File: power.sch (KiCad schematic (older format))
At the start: 51 parts, among them J301 BAT, J302 BAT, J304 SYS, U301 TPS560430X3F, U302 BQ25792

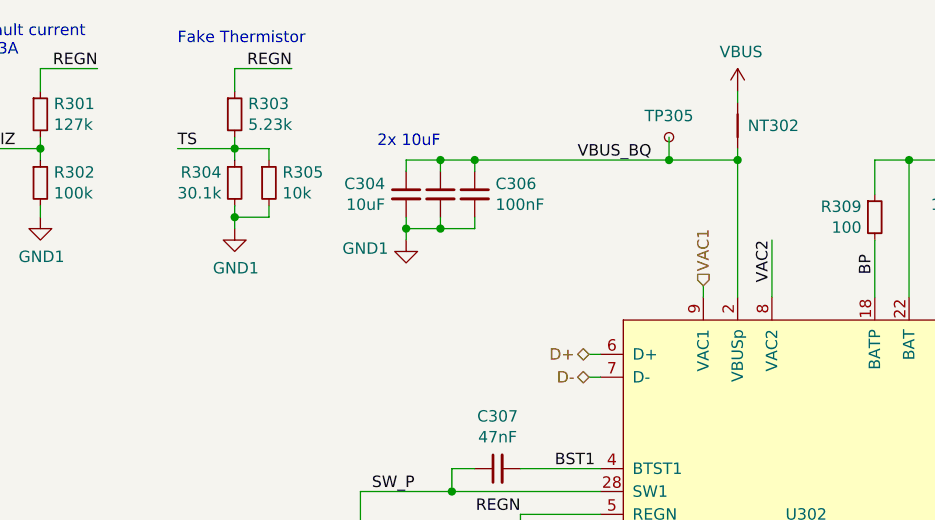
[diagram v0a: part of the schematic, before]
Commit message: added missing JLC/LCSC parts
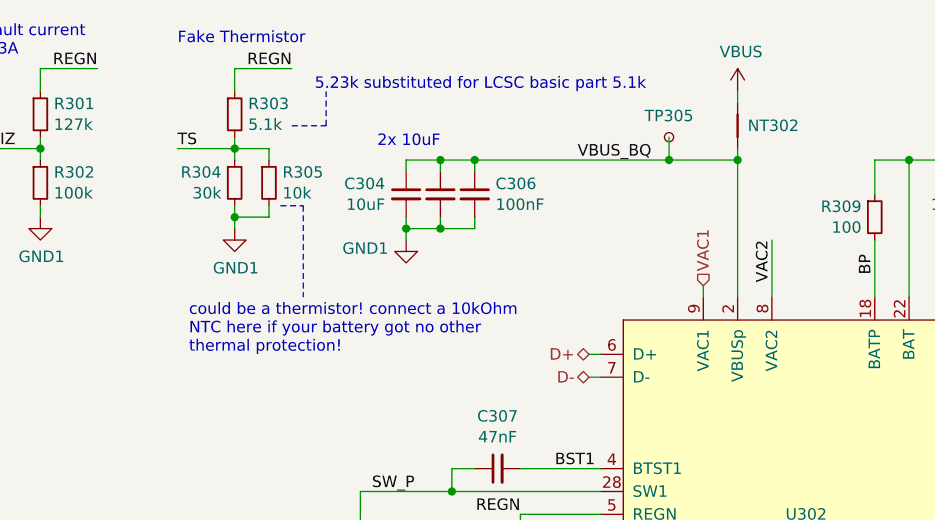
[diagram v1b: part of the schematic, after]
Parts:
- R303: value 5.23k -> 5.1k; JLC (none) -> 0603; LCSC (none) -> C23186
- R304: value 30.1k -> 30k; JLC (none) -> 0603; LCSC (none) -> C22984
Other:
- note added: "5.23k substituted for LCSC basic part 5.1k"
- note added: "could be a thermistor! connect a 10kOhm\nNTC here if your battery got no other\nthermal protection!"
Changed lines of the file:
@@
 P 4300 1750
 F 0 "R303" H 4359 1796 50  0000 L CNN
-F 1 "5.23k" H 4359 1705 50  0000 L CNN
+F 1 "5.1k" H 4359 1705 50  0000 L CNN
 F 2 "Resistor_SMD:R_0603_1608Metric" H 4300 1750 50  0001 C CNN
 F 3 "~" H 4300 1750 50  0001 C CNN
+F 4 "0603" H 4300 1750 50  0001 C CNN "JLC"
+F 5 "C23186" H 4300 1750 50  0001 C CNN "LCSC"
 	1    4300 1750
 	1    0    0    -1
@@
 P 4300 2050
 F 0 "R304" H 4242 2096 50  0000 R CNN
-F 1 "30.1k" H 4242 2005 50  0000 R CNN
+F 1 "30k" H 4242 2005 50  0000 R CNN
 F 2 "Resistor_SMD:R_0603_1608Metric" H 4300 2050 50  0001 C CNN
 F 3 "~" H 4300 2050 50  0001 C CNN
+F 4 " C22984" H 4300 2050 50  0001 C CNN "LCSC"
+F 5 "0603" H 4300 2050 50  0001 C CNN "JLC"
 	1    4300 2050
 	1    0    0    -1
@@
 Wire Wire Line
 	9350 4000 9750 4000
+Text Notes 4650 1650 0    50   ~ 0
+5.23k substituted for LCSC basic part 5.1k
+Wire Notes Line
+	4550 1800 4700 1800
+Wire Notes Line
+	4700 1800 4700 1650
+Text Notes 4100 2800 0    50   ~ 0
+could be a thermistor! connect a 10kOhm\nNTC here if your battery got no other\nthermal protection!
+Wire Notes Line
+	4500 2150 4600 2150
+Wire Notes Line
+	4600 2150 4600 2550
 $EndSCHEMATC

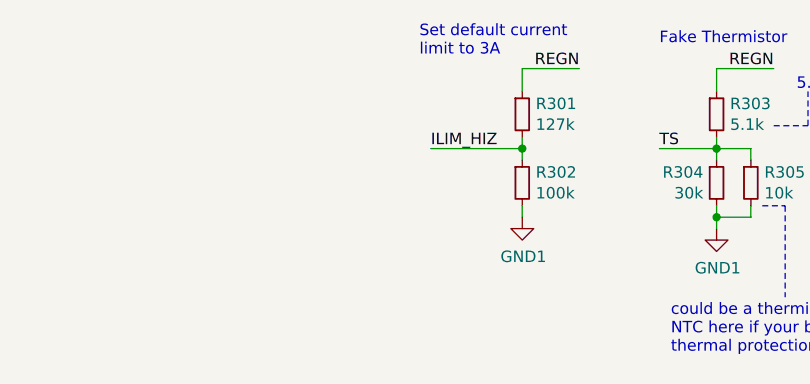
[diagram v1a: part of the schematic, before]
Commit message: changed 127k to 120k
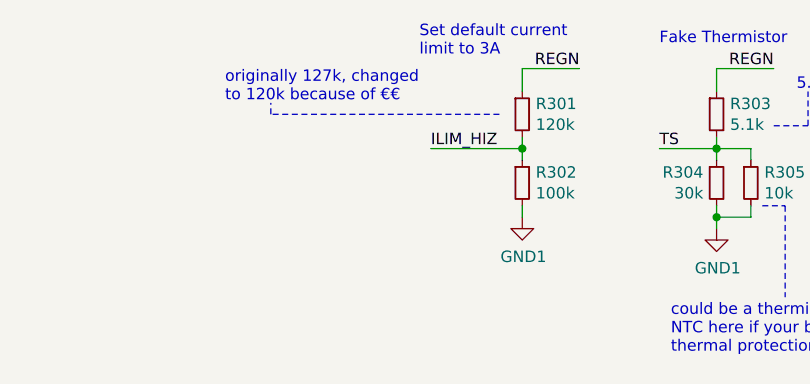
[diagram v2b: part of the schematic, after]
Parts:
- R301: value 127k -> 120k; JLC (none) -> 0603; LCSC (none) -> C25808
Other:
- note added: "originally 127k, changed \nto 120k because of €€"
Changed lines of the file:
@@
 P 3450 1750
 F 0 "R301" H 3509 1796 50  0000 L CNN
-F 1 "127k" H 3509 1705 50  0000 L CNN
+F 1 "120k" H 3509 1705 50  0000 L CNN
 F 2 "Resistor_SMD:R_0603_1608Metric" H 3450 1750 50  0001 C CNN
 F 3 "~" H 3450 1750 50  0001 C CNN
+F 4 "0603" H 3450 1750 50  0001 C CNN "JLC"
+F 5 "C25808" H 3450 1750 50  0001 C CNN "LCSC"
 	1    3450 1750
 	1    0    0    -1
@@
 Wire Notes Line
 	4600 2150 4600 2550
+Text Notes 2150 1700 0    50   ~ 0
+originally 127k, changed \nto 120k because of €€
+Wire Notes Line
+	3350 1750 2350 1750
+Wire Notes Line
+	2350 1750 2350 1700
 $EndSCHEMATC

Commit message: added 3D models
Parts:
- L302: footprint Inductor_SMD:L_Bourns_SRP1245A -> Automated:L_Bourns_SRP1245A
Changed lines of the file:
@@
 F 0 "L302" H 4937 3654 50  0000 L CNN
 F 1 "1uH" H 4937 3745 50  0000 L CNN
-F 2 "Inductor_SMD:L_Bourns_SRP1245A" H 4850 3700 50  0001 C CNN
+F 2 "Automated:L_Bourns_SRP1245A" H 4850 3700 50  0001 C CNN
 F 3 "https://www.bourns.com/data/global/pdfs/SRP1265A.pdf" H 4850 3700 50  0001 C CNN
 F 4 "SRP1265A-1R0M" H 4850 3700 50  0001 C CNN "MPN"
